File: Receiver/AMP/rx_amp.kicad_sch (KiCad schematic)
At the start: 12 parts, among them IC1 BGA616H6327XTSA1, J1 Conn_Coaxial, J2 Conn_Coaxial, J3 Screw_Terminal_01x02

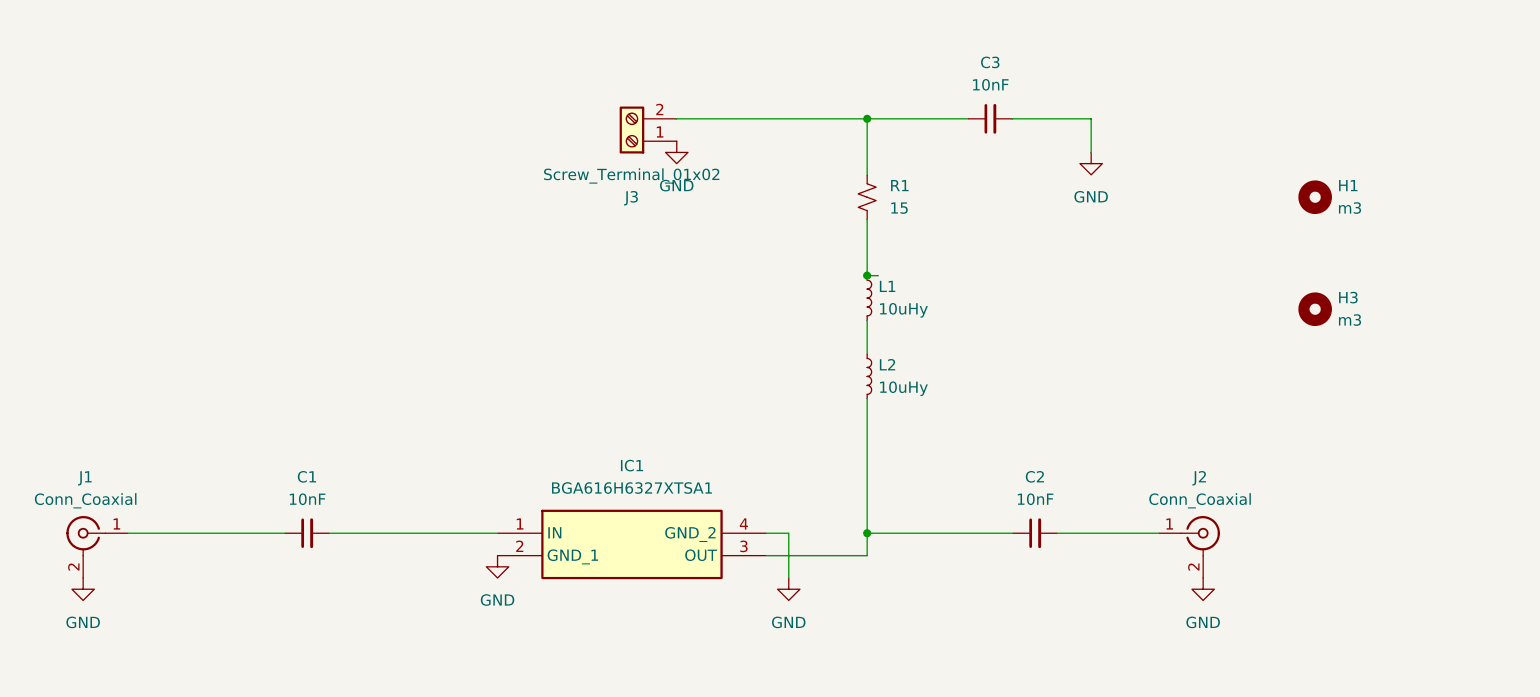
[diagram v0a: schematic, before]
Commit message: Updated Rx Symbol Fields.
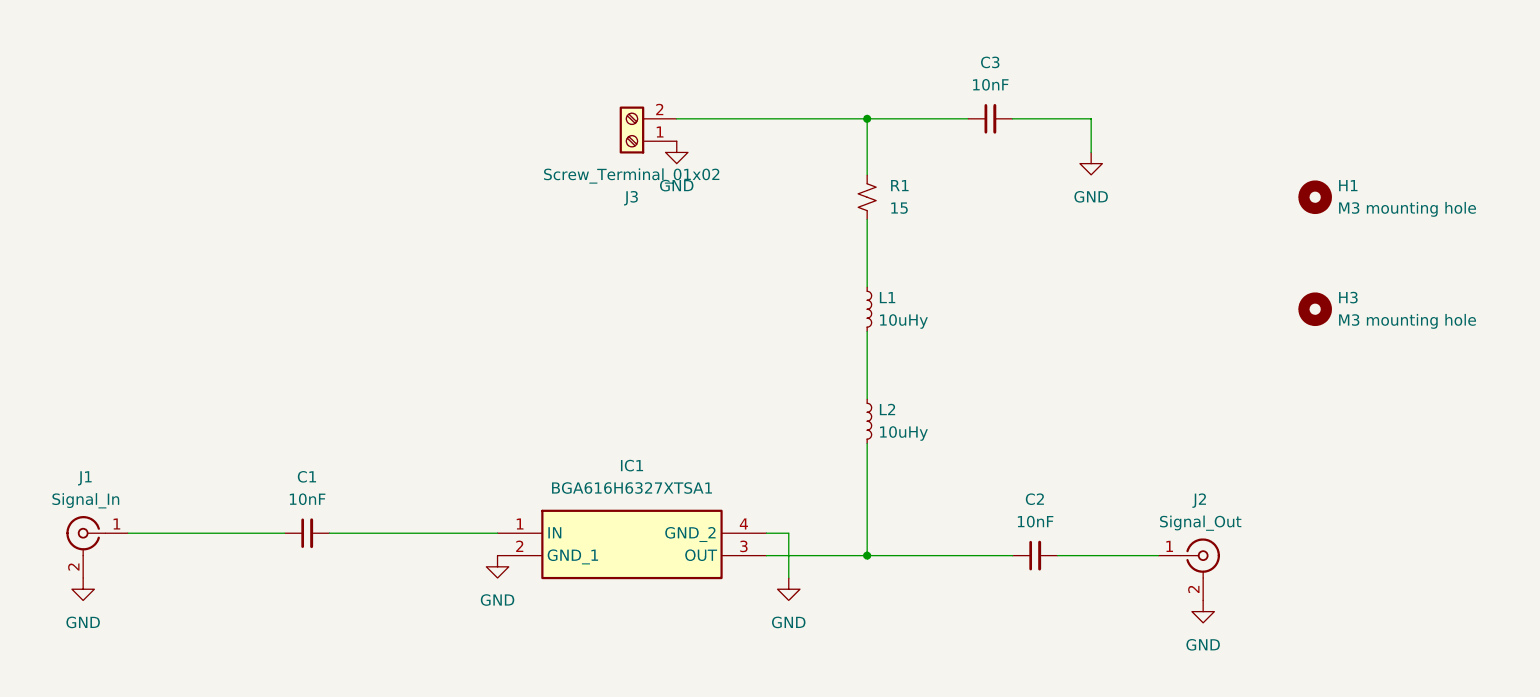
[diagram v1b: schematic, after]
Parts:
- C1, C2, C3: footprint Capacitor_SMD:C_0603_1608Metric_Pad1.08x0.95mm_HandSolder -> Capacitor_SMD:C_0402_1005Metric_Pad0.74x0.62mm_HandSolder; Manufacturer_Name (none) -> KYOCERA AVX; Manufacturer_Part_Number (none) -> 520L103KT16T; Mouser Part Number (none) -> 581-520L103KT16T
- H1, H3: value m3 -> M3 mounting hole
- J1: value Conn_Coaxial -> Signal_In
- J2: value Conn_Coaxial -> Signal_Out
- L1, L2: Manufacturer_Name (none) -> Murata Electronics; Manufacturer_Part_Number (none) -> LQM18DZ100M70L; Mouser Part Number (none) -> 81-LQM18DZ100M70L
- R1: Manufacturer_Name (none) -> Wurth Elektronik; Manufacturer_Part_Number (none) -> 560112116150; Mouser Part Number (none) -> 710-560112116150
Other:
- moved on the sheet: C2, J2, L1, L2

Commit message: Rx Amp first version
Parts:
- added L3: Ferrite Beads 220 OHM, Inductor_SMD:L_0603_1608Metric_Pad1.05x0.95mm_HandSolder, symbol Device:L_Ferrite_Small
- C1, C2, C3: value 10nF -> .1uF; Manufacturer (none) -> KYOCERA AVX; Manufacturer Part Number (none) -> 530L104KT16; Manufacturer_Name KYOCERA AVX -> (none); Manufacturer_Part_Number 520L103KT16T -> (none); Mouser Part Number 581-520L103KT16T -> 581-530L104KT16
- IC1: Height 1 -> (none); Manufacturer (none) -> Infineon; Manufacturer Part Number (none) -> BGA616H6327XTSA1; Manufacturer_Name Infineon -> (none); Manufacturer_Part_Number BGA616H6327XTSA1 -> (none); Mouser Price/Stock https://www.mouser.co.uk/ProductDetail/Infineon-Technologie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 -> (none)
- L1, L2: Manufacturer (none) -> Murata Electronics; Manufacturer Part Number (none) -> LQM18DZ100M70L; Manufacturer_Name Murata Electronics -> (none); Manufacturer_Part_Number LQM18DZ100M70L -> (none)
- R1: Manufacturer (none) -> Wurth Elektronik; Manufacturer Part Number (none) -> 560112116150; Manufacturer_Name Wurth Elektronik -> (none); Manufacturer_Part_Number 560112116150 -> (none)
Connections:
- net at C3.1, R1.1: now also L3.2; no longer J3.2 (Pin_2)
- new net: J3.2 (Pin_2), L3.1
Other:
- moved on the sheet: C2, C3, IC1, J3

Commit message: SMA footprint rx-amp fixed
SMA footprint rx-amp fixed
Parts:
- J1, J2: footprint rx_amp:RFSOLUTIONS_CON-SMA-EDGE-S -> Connector_Coaxial:SMA_Samtec_SMA-J-P-X-ST-EM1_EdgeMount
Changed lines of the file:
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@@
 			)
 		)
-		(property "Footprint" "rx_amp:RFSOLUTIONS_CON-SMA-EDGE-S"
+		(property "Footprint" "Connector_Coaxial:SMA_Samtec_SMA-J-P-X-ST-EM1_EdgeMount"
 			(at 215.9 104.14 0)
 			(effects
@@
 			)
 		)
-		(property "Footprint" "rx_amp:RFSOLUTIONS_CON-SMA-EDGE-S"
+		(property "Footprint" "Connector_Coaxial:SMA_Samtec_SMA-J-P-X-ST-EM1_EdgeMount"
 			(at 88.9 101.6 0)
 			(effects
